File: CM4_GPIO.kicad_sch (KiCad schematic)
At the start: 22 parts, among them IC5 74LVC1G07QSE-7, J3 THD-20-R, SW1 SW_Push, SW2 SW_Push, SW3 SW_DPDT_x2, SW4 SW_DPDT_x2, SW5 SW_Push

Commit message: small changes for ravi
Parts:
- removed C10, C11, C6, C7, C8, C9: 100n, Capacitor_SMD:C_0402_1005Metric, symbol Device:C
- removed C3, C5: 10u, Capacitor_SMD:C_0805_2012Metric, symbol Device:C
- added D5: 3.3V, LED_SMD:LED_0805_2012Metric, symbol Device:LED
- added R25: 700, Resistor_SMD:R_0805_2012Metric, symbol Device:R
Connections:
- net +3.3V_PWR: now also R25.1
- net GND: now also D5.1 (K)
- new net: D5.2 (A), R25.2
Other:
- note added: "5V PWR"
- moved on the sheet: SW3A, SW3B, SW4A, SW4B

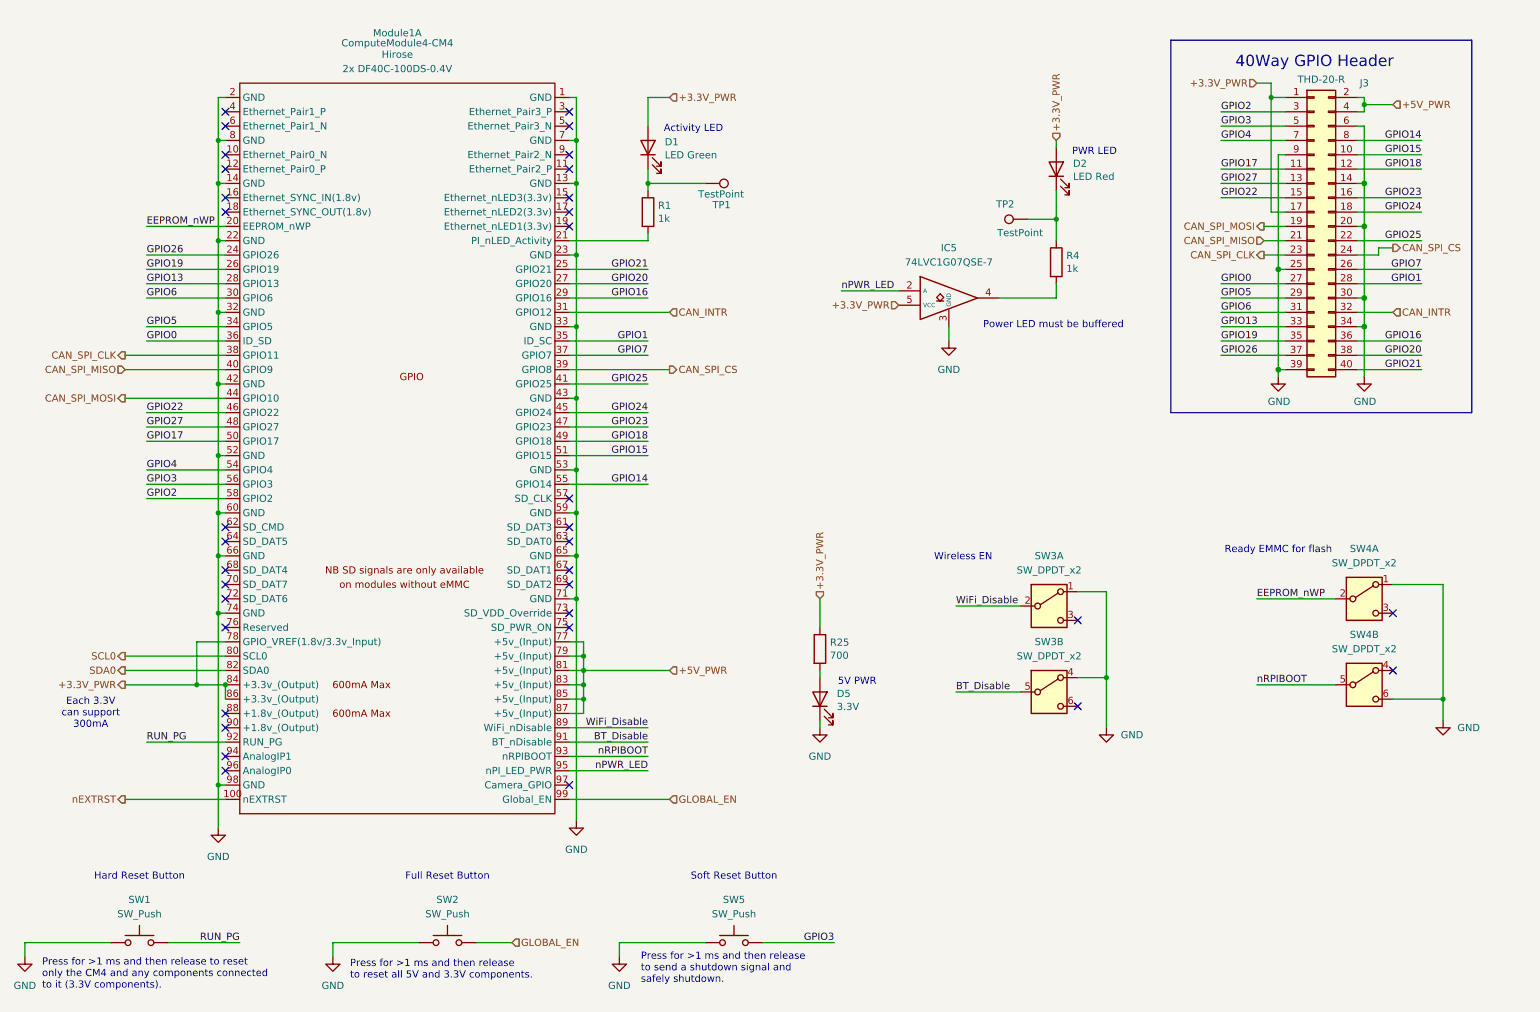
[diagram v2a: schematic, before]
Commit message: added parts to almost everything (except can xtal and fuses)
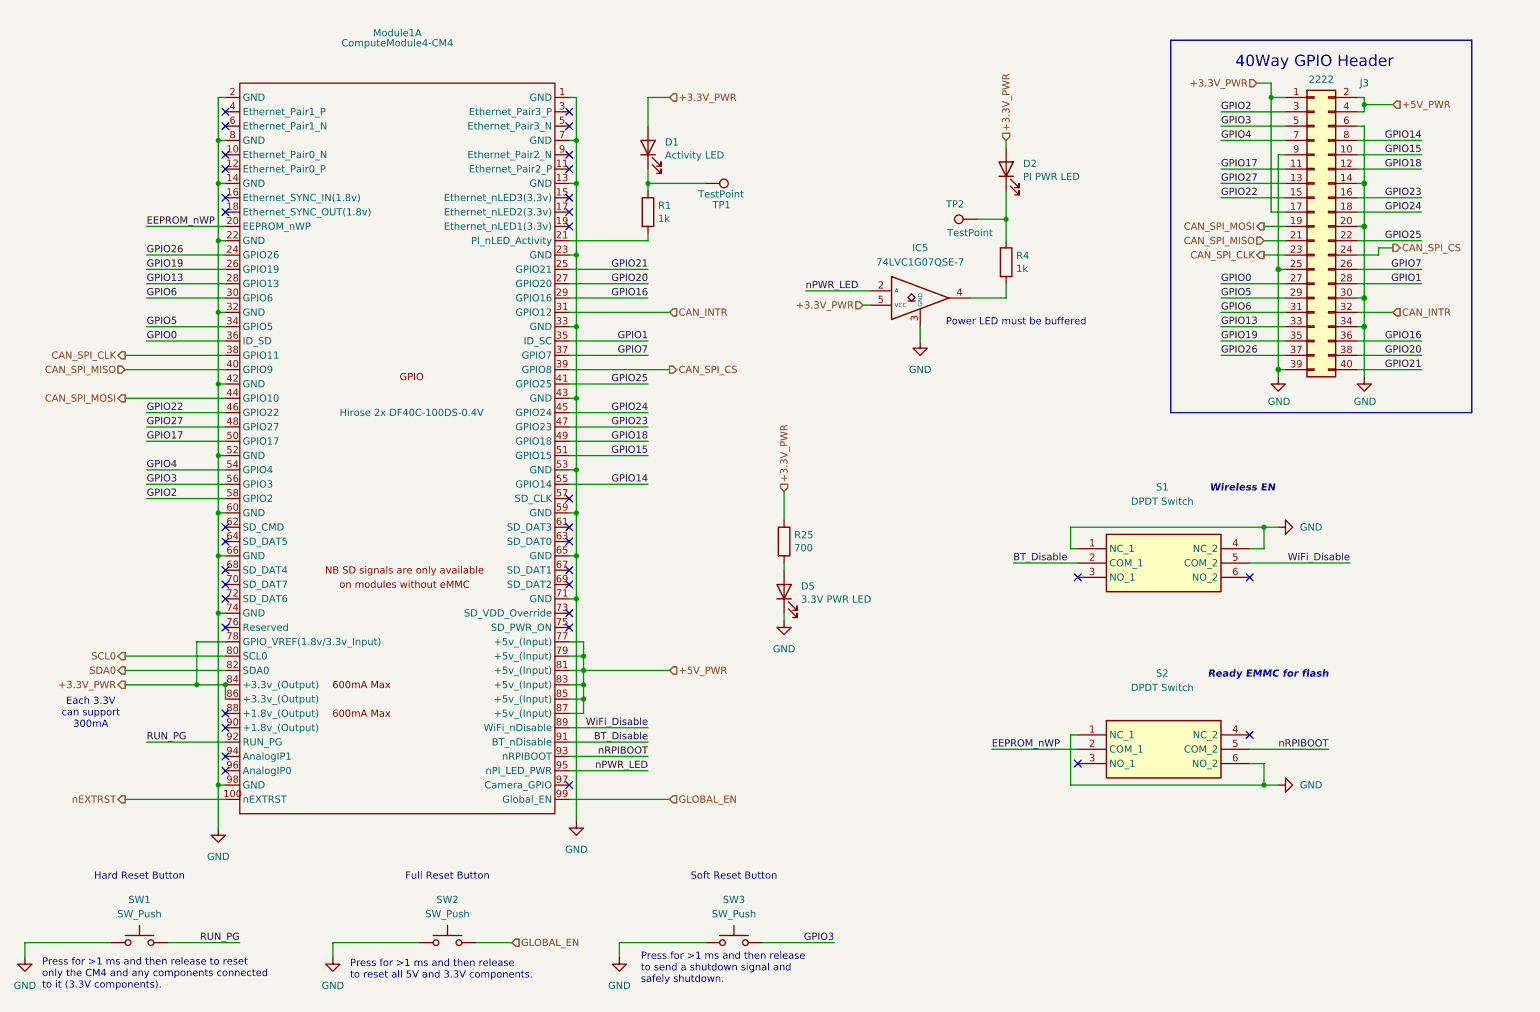
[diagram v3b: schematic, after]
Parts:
- removed SW3, SW4: SW_DPDT_x2, symbol Switch:SW_DPDT_x2
- removed SW5: SW_Push, symbol Switch:SW_Push
- added S1, S2: DPDT Switch, Controls_Pi:CLSB22B12T, symbol CL-SB-22B-12T:CL-SB-22B-12T
- added SW3: SW_Push, Button_Switch_SMD:SW_SPST_B3SL-1002P, symbol Switch:SW_Push
- D1: value LED Green -> Activity LED; footprint LED_SMD:LED_0603_1608Metric -> LED_SMD:LED_0805_2012Metric; Field4 Digikey -> (none); Field5 LTST-S270KGKT -> (none); Field6 SML-A12M8TT86N -> (none); Field7 Rohm -> (none); Field8 650263301 -> (none); P/N (none) -> APTD2012LCGCK; Part Description Green 572nm LED Indication - Discrete 2.2V 2-SMD, No Lead -> (none)
- D2: value LED Red -> PI PWR LED; footprint LED_SMD:LED_0603_1608Metric -> LED_SMD:LED_0805_2012Metric; Field4 Digikey -> (none); Field5 LTST-S270KRKT -> (none); Field6 SML-A12U8TT86Q -> (none); Field7 Rohm -> (none); Field8 650295101 -> (none); P/N (none) -> APTD2012LSURCK; Part Description Red 620nm LED Indication - Discrete 2.2V 2-SMD, No Lead -> (none)
- D5: value 3.3V -> 3.3V PWR LED; Color Green -> (none); If 2mA -> (none); Mouser Part Number 604-APTD2012LCGCK -> (none); Vf 1.9V -> (none)
- IC5: Arrow Part Number 74LVC1G07QSE-7 -> (none); Arrow Price/Stock https://www.arrow.com/en/products/74lvc1g07qse-7/diodes-inc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 -> (none); Height 1.1 -> (none); Manufacturer_Name Diodes Incorporated -> (none); Manufacturer_Part_Number 74LVC1G07QSE-7 -> (none); Mouser Part Number 621-74LVC1G07QSE-7 -> (none); Mouser Price/Stock https://www.mouser.co.uk/ProductDetail/Diodes-Incorporated/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 -> (none); P/N (none) -> 74LVC1G07QSE-7
- J3: value THD-20-R -> 2222; footprint Connector_PinHeader_2.54mm:PinHeader_2x20_P2.54mm_Vertical -> Connector_PinSocket_2.54mm:PinSocket_2x20_P2.54mm_Vertical; Field4 Toby -> (none); Field5 THD-20-R -> (none); Field6 THD-20-R -> (none); Field7 Toby -> (none); Field8 UCON00511 -> (none); P/N (none) -> 2222; Part Description PinHeader_2x20_P2.54mm_Vertical -> (none)
- Module1: Field4 Hirose -> (none); Field5 2x DF40C-100DS-0.4V -> (none); P/N (none) -> DF40C-100DS-0.4V(51)
- R1, R4: footprint Resistor_SMD:R_0402_1005Metric -> Resistor_SMD:R_0805_2012Metric; Field4 Farnell -> (none); Field5 9239235 -> (none); Field6 RK73H1ETTP1001F -> (none); Field7 KOA EUROPE GMBH -> (none); Field8 125049511 -> (none); P/N (none) -> CRCW08051K00FKEAC; Part Description Resistor 1K M1005 1% 63mW -> (none)
- R25: Mouser Part Number Inventory -> (none); P/N SDR10EZPF2200 -> ERJ-P06F7150V
- SW1, SW2: footprint (none) -> Button_Switch_SMD:SW_SPST_B3SL-1002P; P/N (none) -> 653-B3SL-1002P
- TP1, TP2: Field4 nf -> (none); Field5 nf -> (none); Field6 nf -> (none); Field7 nf -> (none)
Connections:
- net BT_Disable: now also S1.2 (COM_1)
- net EEPROM_nWP: now also S2.2 (COM_1)
- net GND: now also S1.1 (NC_1), S1.4 (NC_2), S2.1 (NC_1), S2.6 (NO_2), SW3.1
- net GPIO3: now also SW3.2
- net WiFi_Disable: now also S1.5 (COM_2)
- net nRPIBOOT: now also S2.5 (COM_2)
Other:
- note removed: "5V PWR"
- note removed: "Activity LED"
- note removed: "PWR LED"
- moved on the sheet: IC5, R25, TP2

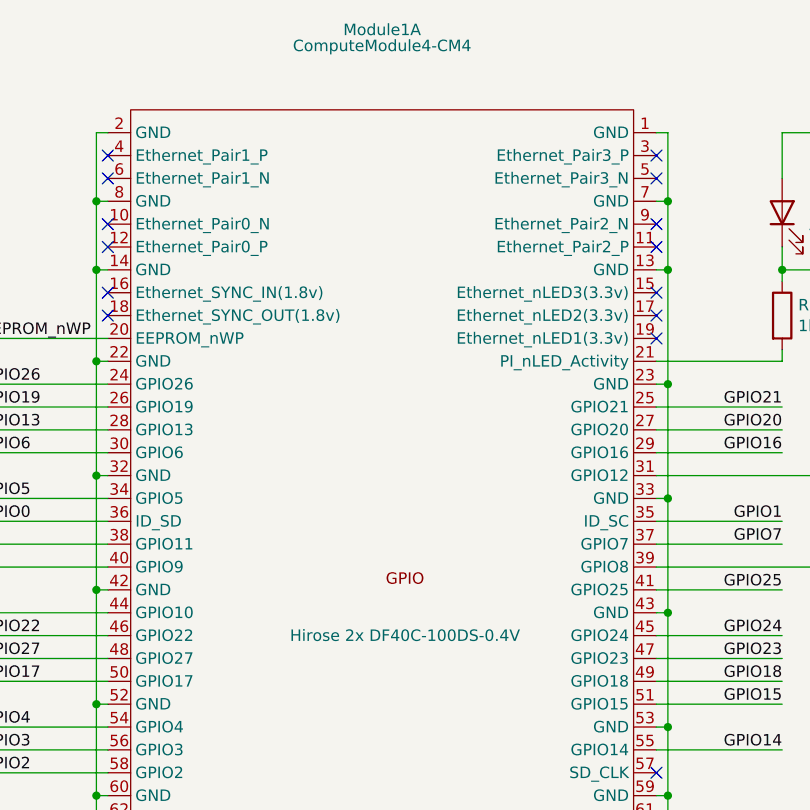
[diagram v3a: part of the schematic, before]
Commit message: fixed cap sizes, added remaining parts, fixed rtc battery
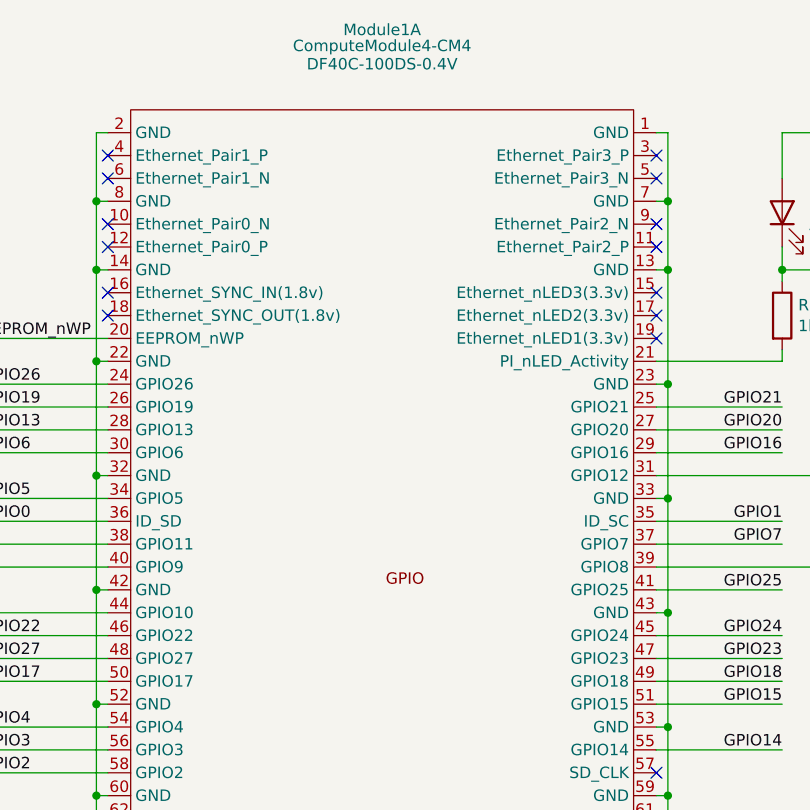
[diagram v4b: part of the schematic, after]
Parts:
- IC5: footprint SOT65P210X110-5N -> Controls_Pi:SOT65P210X110-5N
- Module1: P/N DF40C-100DS-0.4V(51) -> DF40C-100DS-0.4V
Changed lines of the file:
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@@
 			)
 		)
-		(property "Footprint" "SOT65P210X110-5N"
+		(property "Footprint" "Controls_Pi:SOT65P210X110-5N"
 			(at 193.04 160.96 0)
 			(effects
@@
 				(font
 					(size 1.27 1.27)
-				)
-				(hide yes)
-			)
-		)
-		(property "Description" "Hirose 2x DF40C-100DS-0.4V"
+					(italic yes)
+				)
+				(hide yes)
+			)
+		)
+		(property "Description" "100 Position Connector Receptacle, Center Strip Contacts Surface Mount Gold"
 			(at 86.36 86.36 0)
 			(effects
@@
 					(size 1.27 1.27)
 				)
-			)
-		)
-		(property "P/N" " DF40C-100DS-0.4V(51) "
+				(hide yes)
+			)
+		)
+		(property "P/N" "DF40C-100DS-0.4V"
 			(at 83.82 22.86 0)
 			(effects
@@
 					(size 1.27 1.27)
 				)
-				(hide yes)
-			)
-		)
+			)
+		)

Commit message: review committee changes implmented
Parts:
- added C22, C23, C51: 100n, Capacitor_SMD:C_0805_2012Metric, symbol Device:C
- added R17, R19, R22: 1k, Resistor_SMD:R_0805_2012Metric, symbol Device:R
- added R18, R21, R23, R26, R29: 10k, Resistor_SMD:R_0805_2012Metric, symbol Device:R
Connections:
- net +3.3V_PWR: now also R26.1, R29.1
- net +5V_PWR: now also R18.1, R21.1, R23.1
- net GLOBAL_EN: now also C23.1, R19.2, R21.2; no longer SW2.2
- net GND: now also C22.2, C23.2, C51.2
- net GPIO3: now also C51.1, R22.2, R23.2; no longer SW3.2
- net RUN_PG: now also C22.1, R17.2, R18.2; no longer SW1.2
- net SCL0: now also R26.2
- net SDA0: now also R29.2
- new net: R17.1, SW1.2
- new net: R19.1, SW2.2
- new net: R22.1, SW3.2
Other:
- note added: "I2C Pullups"
- moved on the sheet: D1, D2, D5, IC5, J3, Module1A, R1, R25, R4, S1, S2, SW1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

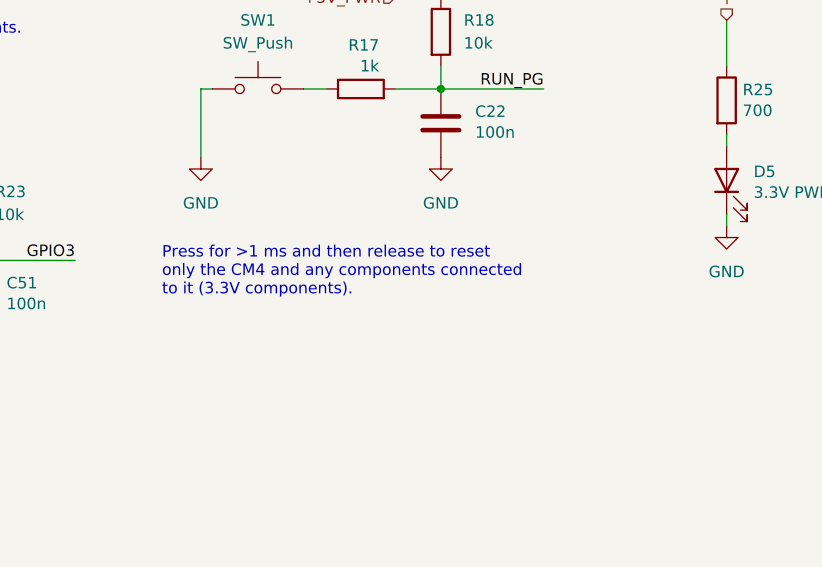
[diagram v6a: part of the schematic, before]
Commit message: Migrate to USB C and added some ESD protections on Vbus; might still have some issues
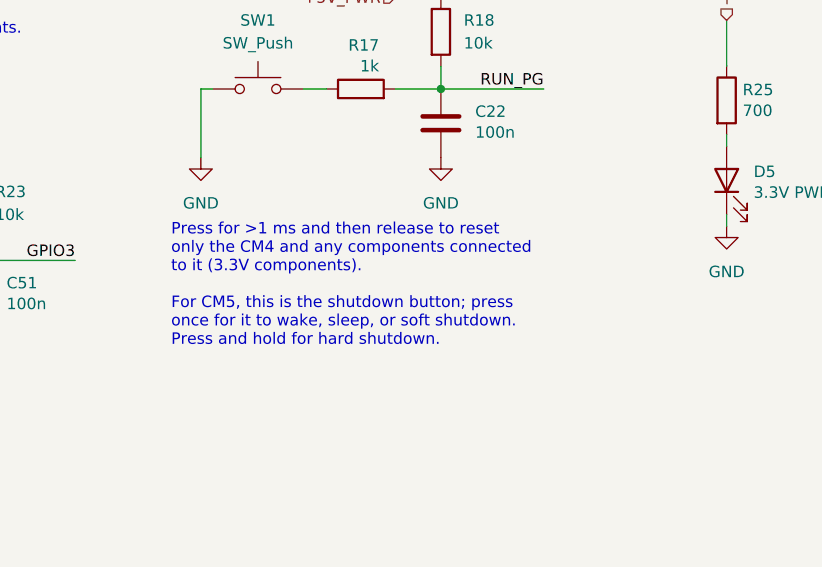
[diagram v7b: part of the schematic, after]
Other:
- note added: "Press for >1 ms and then release to reset only the CM4 and any components connected to it (3.3V components). For CM5, this is the shutdown button; press once for it to wake, sleep, or soft shutdown. Press and hold for hard shutdown."
- note removed: "Press for >1 ms and then release to reset only the CM4 and any components connected to it (3.3V components)."

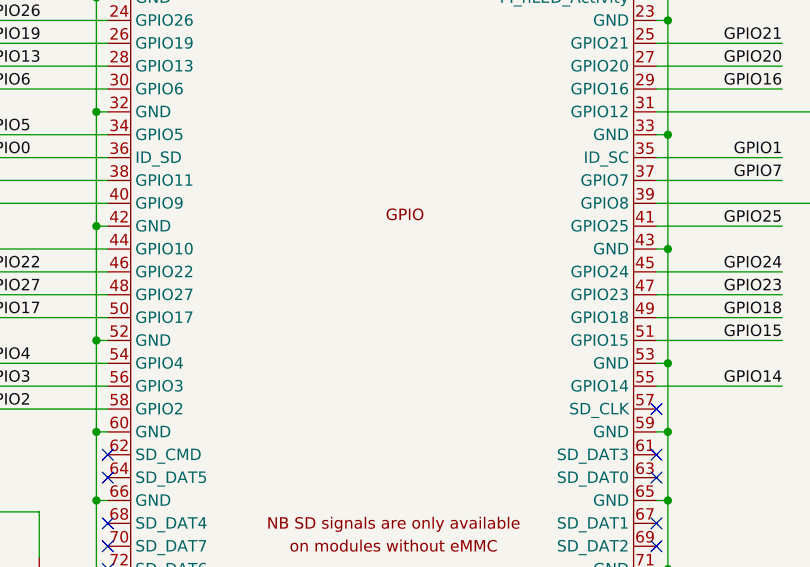
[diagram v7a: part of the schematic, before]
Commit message: fixed erc and removed old schematics
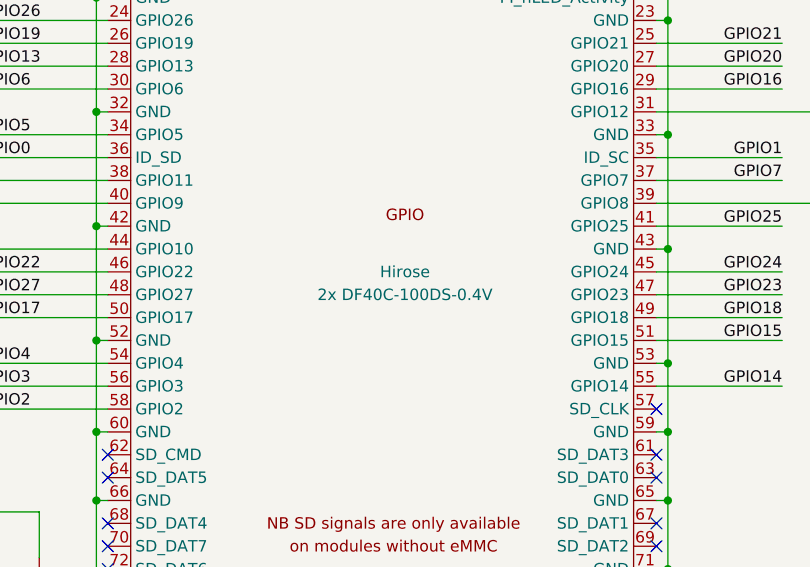
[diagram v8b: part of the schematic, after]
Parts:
- IC5: Arrow Part Number (none) -> 74LVC1G07QSE-7; Arrow Price/Stock (none) -> https://www.arrow.com/en/products/74lvc1g07qse-7/diodes-inc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; Height (none) -> 1.1; Manufacturer_Name (none) -> Diodes Incorporated; Manufacturer_Part_Number (none) -> 74LVC1G07QSE-7; Mouser Part Number (none) -> 621-74LVC1G07QSE-7; Mouser Price/Stock (none) -> https://www.mouser.co.uk/ProductDetail/Diodes-Incorporated/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
- Module1: Field4 (none) -> Hirose; Field5 (none) -> 2x DF40C-100DS-0.4V
- S1, S2: Height (none) -> 3.5
